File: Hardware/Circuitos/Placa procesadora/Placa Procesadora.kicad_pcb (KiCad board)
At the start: 2 copper layers, 46 x 45 mm, 26 parts, among them J1 Conn_01x02, J2 Conn_01x02, J7 Conn_01x02, U1 LM358

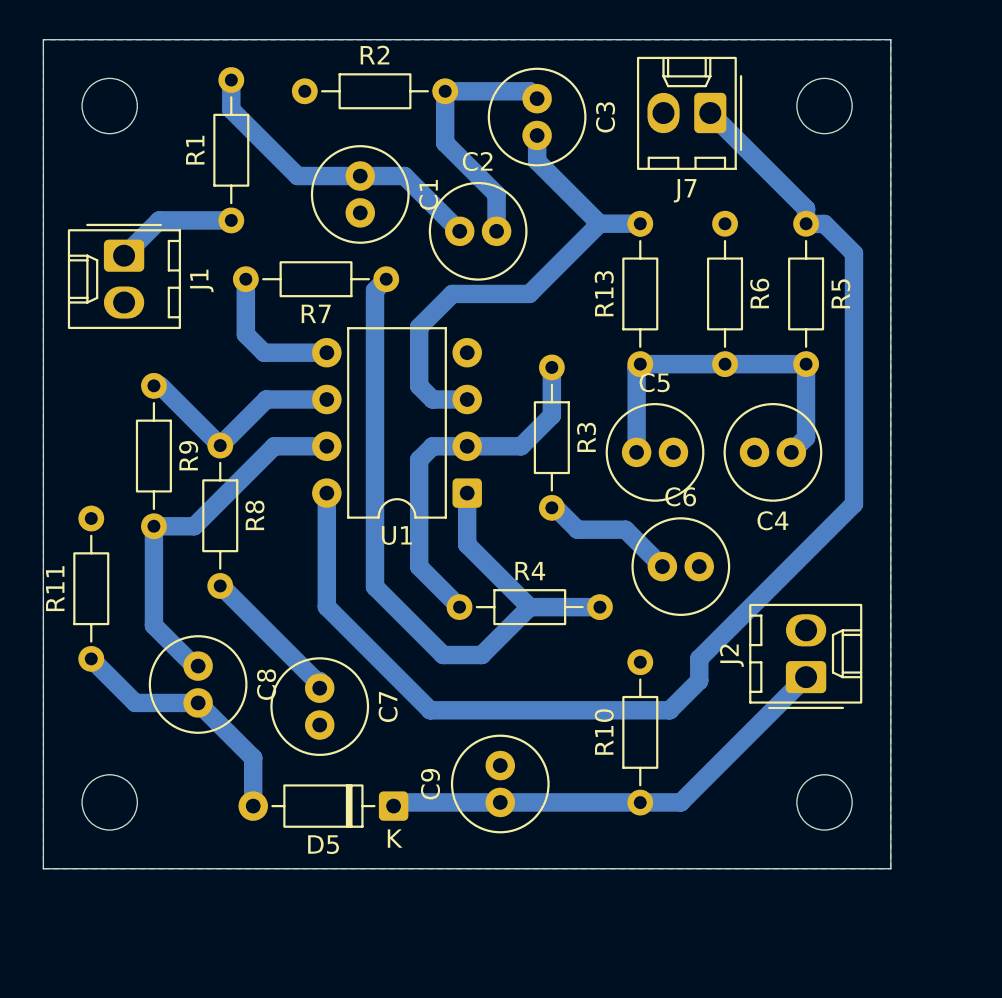
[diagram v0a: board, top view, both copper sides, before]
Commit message: Placa procesadora - Corrección de tamaño
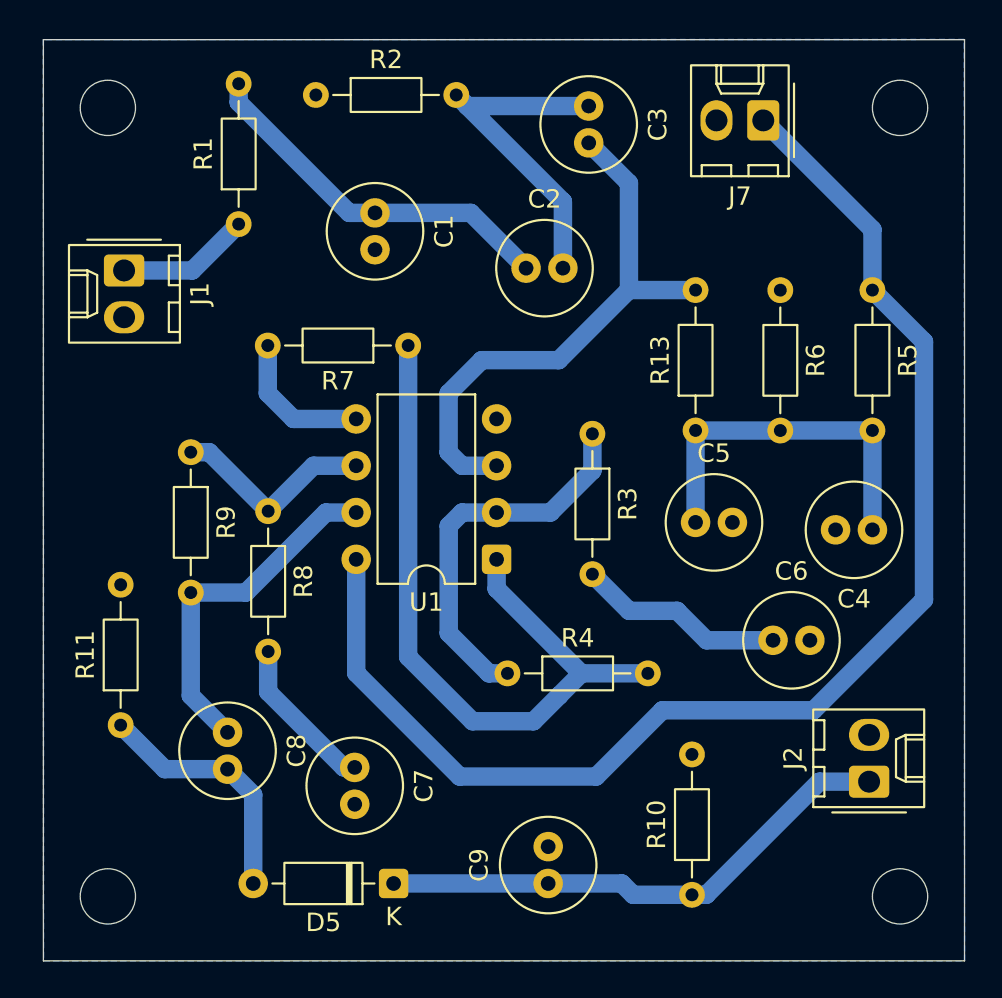
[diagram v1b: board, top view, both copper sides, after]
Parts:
- moved C6 7.22 mm to (150.6, 67.4)
- moved J2 6.63 mm to (155.8, 75.1)
- moved C4 6.09 mm to (156.0, 61.4)
- moved R10 5.74 mm to (146.2, 81.2)
- moved C9 5.11 mm to (138.4, 80.6)
- moved R5 5.09 mm to (156.0, 48.4)
- moved C5 4.97 mm to (146.4, 61.0)
- moved C7 4.70 mm to (127.9, 74.3)
- moved R6 4.69 mm to (151.0, 48.4)
- moved R13 4.69 mm to (146.4, 56.0)
- moved R4 4.44 mm to (136.2, 69.2)
- moved R8 4.41 mm to (123.2, 60.4)
- moved R3 4.22 mm to (140.8, 56.2)
- moved D5 4.20 mm to (130.0, 80.6)
- moved C2 4.12 mm to (137.2, 47.2)
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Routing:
- net /5V: track 67.5 -> 72.9 mm
- net Net-(C2-Pad2): track 13.9 -> 18.4 mm
- net Net-(C6-Pad1): track 7.32 -> 11.3 mm
- net Net-(U1A-+): track 26.8 -> 30.7 mm
- net Net-(C1-Pad1): track 16.7 -> 20.3 mm
- net Net-(D5-K): track 25.3 -> 28.6 mm
- net Net-(U1A--): track 19.7 -> 21.0 mm
- net Net-(C7-Pad1): track 7.48 -> 8.59 mm
- net Net-(C4-Pad1): track 19.0 -> 20.0 mm
- net Net-(R4-Pad2): track 39.4 -> 40.1 mm
- net Net-(D5-A): track 13.6 -> 13.0 mm
- net Net-(J1-Pin_1): track 6.61 -> 7.26 mm
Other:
- board size 46 x 45 mm -> 50 x 50 mm
